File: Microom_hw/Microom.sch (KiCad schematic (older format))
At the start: 56 parts

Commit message: Sch 50% complete
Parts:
- removed R? (x8): 200, symbol R
- added C? (x3): 0.1u, CAP_0603, symbol C
- added C? (x2): 1u, CAP_0603, symbol C
- added C? (x2): 10u, CAP_0603, symbol C
- added DA?: PCM1865, TSSOP30, symbol PCM1865
- added F?: Fuse0R, symbol Fuse0R
- added R? (x8): 510, symbol R
- added TP? (x9): TESTPOINT, symbol TESTPOINT
- R?: value 200 -> 510
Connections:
- net labels added: +3.3V_A, 1V8, AGND, BitClk, CS, DataOut, LRClk, MCO, MISO, MOSI, SCK, SCKI
- net labels removed: VAA
- wire segments 141 -> 187
- no-connect marks 31 -> 30
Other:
- note added: "I2S2 WS (NSS)"
- note added: "I2S_MCK"
- note added: "No Crystal"
- note added: "SPI"
- moved on the sheet: R?

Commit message: Sch 100% completed
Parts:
- removed HOLE?: HOLE_METALLED, symbol HOLE_METALLED
- added C21, C28, C31: 2.2u, CAP_0603, symbol C
- added C22, C23, C29, C32, C33: 0.1u, CAP_0603, symbol C
- added C26: 1u, CAP_0603, symbol C
- added C27, C35: 10u, CAP_0603, symbol C
- added C36, C37, C38, C39, C40, C41, C42, C43: 10n, CAP_0603, symbol C
- added C44, C45, C46, C47, C48, C49, C50, C51: 10u, CAP_0805, symbol C
- added DA4: PCM1865, TSSOP30, symbol PCM1865
- added MIC1, MIC2, MIC3, MIC4, MIC5, MIC6, MIC7, MIC8: Microphone, symbol Microphone
- added R14, R15, R16, R17, R18, R19, R20, R21: 100R, RES_0603, symbol R
- added R22, R23, R24, R25, R26, R27, R28, R29: 2.2k, RES_0603, symbol R
- added R30, R31, R32, R33, R34, R35, R36, R37: 100k, RES_0603, symbol R
- added TP1, TP11, TP12, TP13, TP14, TP15, TP16, TP17, TP18, TP19, TP20: TESTPOINT, symbol TESTPOINT
- C18: renamed from C?; value 1u -> 2.2u
- gave numbers to parts that had none: 72
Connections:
- net +3.3V_A: now also C23.1, C27.1, C33.1, C35.1, DA4.13 (DVDD), DA4.14 (IOVDD), DA4.26 (MD0), DA4.8 (AVDD)
- net 1V8: now also C22.1, C26.1, DA4.11 (LDO)
- net AGND: now also C21.2, C22.2, C23.2, C26.2, C27.2, C28.2, C29.2, C31.2, C32.2, C33.2, C35.2, C36.2, C37.2, C38.2, C39.2, C40.2, C41.2, C42.2, C43.2, DA4.10 (XI), DA4.12 (DGND), DA4.7 (AGND), MIC1.2, MIC2.2, MIC3.2, MIC4.2, MIC5.2, MIC6.2, MIC7.2, MIC8.2, R30.2, R31.2, R32.2, R33.2, R34.2, R35.2, R36.2, R37.2
- net GND: no longer HOLE1.H, HOLE2.H, HOLE3.H
- net LED1: now also DD1.9 ((ADC123-11)/PC1)
- net LED2: now also DD1.10 ((ADC123-12)/MISO2/PC2)
- net LED3: now also DD1.11 ((ADC123-13)/MOSI2/PC3)
- net LED4: now also DD1.24 ((ADC12-14)/PC4)
- net LED5: now also DD1.25 ((ADC12-15)/PC5)
- net LED6: now also DD1.38 (T8C2/RX6/T3C2/SDIO_D7/PC7)
- net LED7: now also DD1.39 (T8C3/T3C3/CK6/SDIO_D0/PC8)
- net LED8: now also DD1.2 (PC13)
- net LED_AUX: now also DD1.8 ((ADC123-10)/PC0)
- net MISO: now also DA4.22 (MISO/GPIO0/DMIN2)
- net MOSI: now also DA4.23 (MOSI/SDA)
- net SCK: now also DA4.24 (MC/SCL)
- net SCKI: now also DA4.15 (SCKI)
- net GPIO22: now reaches DD1.14 ((ADC123-0)/TX4/T5C1/WKUP/PA0)
- net GPIO22: now also DA4.20 (GPIO2/IntB/DMCLK), TP19.1
- net GPIO32: now reaches DD1.15 ((ADC123-1)/RX4/T5C2/T2C2/PA1)
- net GPIO32: now also DA4.19 (GPIO3/IntC), TP20.1
- net CS2: now reaches DD1.17 ((ADC123-3)/T5C4/T9C2/T2C4/RX2/PA3)
- net CS2: now also DA4.25 (MS/AD), TP17.1
- net GPIO21: now reaches DD1.26 (PB0/T3C3/(ADC12-8))
- net GPIO21: now also DA3.20 (GPIO2/IntB/DMCLK), TP12.1
- net GPIO31: now reaches DD1.27 (PB1/T3C4/(ADC12-9))
- net GPIO31: now also DA3.19 (GPIO3/IntC), TP13.1
- net GPIO11: now reaches DD1.35 (PB14/MISO2/T12C1)
- net GPIO11: now also DA3.21 (GPIO1/IntA/DMIN), TP11.1
- net MCO2: now reaches DD1.40 (MCO2/T8C4/SDA3/T3C4/SDIO_D1/PC9)
- net MCO2: now also TP1.1
- net LRClk2: now reaches DD1.50 (PA15)
- net LRClk2: now also DA4.16 (LRCK), TP14.1
- net BitClk2: now reaches DD1.51 (SCK3/TX4/TX3/SDIO_D2/PC10)
- net BitClk2: now also DA4.17 (BCK), TP15.1
- net GPIO12: now reaches DD1.52 (MISO3/RX4/RX3/SDIO_D3/PC11)
- net GPIO12: now also DA4.21 (GPIO1/IntA/DMIN), TP18.1
- net DataOut2: now reaches DD1.53 (MOSI3/TX5/CK3/SDIO_CK/PC12)
- net DataOut2: now also DA4.18 (DOUT), TP16.1
- net VinL2: now reaches DA3.1 (VinL2)
- net VinL2: now also C38.1, R16.2
- net VinR2: now reaches DA3.2 (VinR2)
- net VinR2: now also C39.1, R17.2
- net VinL4: now reaches DA3.27 (VinL4)
- net VinL4: now also C42.1, DA4.27 (VinL4), R20.2
- net VinR4: now reaches DA3.28 (VinR4)
- net VinR4: now also C43.1, DA4.28 (VinR4), R21.2
- net VinL3: now reaches DA3.29 (VinL3)
- net VinL3: now also C40.1, DA4.29 (VinL3), R18.2
- net VinL1: now reaches DA3.3 (VinL1)
- net VinL1: now also C36.1, R14.2
- net VinR3: now reaches DA3.30 (VinR3)
- net VinR3: now also C41.1, DA4.30 (VinR3), R19.2
- net VinR1: now reaches DA3.4 (VinR1)
- net VinR1: now also C37.1, R15.2
- net MicBias: now reaches DA3.5 (MicBias)
- net MicBias: now also C28.1, C29.1, R22.2, R23.2, R24.2, R25.2, R26.2, R27.2, R28.2, R29.2
- net BitClk renamed BitClk1
- net CS renamed CS1
- net DataOut renamed DataOut1
- net LRClk renamed LRClk1
- net MCO renamed MCO1
- new net: C44.2, MIC1.1, R22.1, R30.1
- new net: C44.1, R14.1
- new net: C45.2, MIC2.1, R23.1, R31.1
- new net: C45.1, R15.1
- new net: C46.2, MIC3.1, R24.1, R32.1
- new net: C46.1, R16.1
- new net: C47.2, MIC4.1, R25.1, R33.1
- new net: C47.1, R17.1
- new net: C48.2, MIC5.1, R26.1, R34.1
- new net: C48.1, R18.1
- new net: C49.2, MIC6.1, R27.1, R35.1
- new net: C49.1, R19.1
- new net: C50.2, MIC7.1, R28.1, R36.1
- new net: C50.1, R20.1
- new net: C51.2, MIC8.1, R29.1, R37.1
- new net: C51.1, R21.1
- new net: C21.1, DA4.6 (Vref)
- new net MicBias2: C31.1, C32.1, DA4.5 (MicBias)
- no-connect marks 30 -> 23
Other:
- note added: "Audio converters"
- note added: "I2S3 WS (NSS)"
- note added: "Indication and mounting"
- note added: "MCU"
- note added: "Microphones"
- moved on the sheet: C1, C10, C11, C18, C19, C2, C20, C24, C25, C3, C30, C34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

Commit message: PCB routing started, components put on board
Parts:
- removed VCap1, VCap2: 2.2u, symbol C
- added C52, C53: 2.2u, Capacitors:CAP_0603, symbol C
- C1: footprint (none) -> Capacitors:CAP_0805
- C10, C11, C14, C15, C16, C17, C2, C3, C4, C6, C8, C9: footprint (none) -> Capacitors:CAP_0603
- C13, C5, C7: footprint Capacitors:CAP_0402 -> Capacitors:CAP_0603
- C18, C19, C20, C21, C22, C23, C24, C26, C28, C29, C30, C31, C32, C33, C36, C37, C38, C39, C40, C41, C42, C43: footprint CAP_0603 -> Capacitors:CAP_0603
- C25, C27, C34, C35: footprint CAP_0603 -> Capacitors:CAP_0805
- C44, C45, C46, C47, C48, C49, C50, C51: footprint CAP_0805 -> Capacitors:CAP_0805
- D1, D2, D3, D4, D5, D6, D7, D8, D9: footprint (none) -> LEDs:LED_0603
- DA1, DA2: footprint (none) -> SOT:SOT23-5
- DA3, DA4: footprint TSSOP30 -> SO_DIL_TSSOP:TSSOP30
- DD1: footprint (none) -> LQFP_TQFP:LQFP64
- F1: footprint (none) -> Resistors:RES_0603_SOLDERFUSE
- HOLE1, HOLE2, HOLE3: footprint (none) -> PCB:Hole3_5_out6mm
- MIC1, MIC2, MIC3, MIC4, MIC5, MIC6, MIC7, MIC8: footprint (none) -> Connectors:PLS-2
- R1: footprint Resistors:RES_0402 -> Resistors:RES_0603
- R10, R11, R12, R13, R2, R3, R5, R6, R7, R8, R9: footprint (none) -> Resistors:RES_0603
- R14, R15, R16, R17, R18, R19, R20, R21, R22, R23, R24, R25, R26, R27, R28, R29, R30, R31, R32, R33, R34, R35, R36, R37, R4: footprint RES_0603 -> Resistors:RES_0603
- SW1: footprint (none) -> BtnsSwitches:BTN_6x6
- TP1, TP10, TP11, TP12, TP13, TP14, TP15, TP16, TP17, TP18, TP19, TP2, TP20, TP3, TP4, TP5, TP6, TP7, TP8, TP9: footprint (none) -> PCB:TESTPOINT_1MM
- XL1: footprint ~ -> Connectors:PLS-3
- XL3: footprint ~ -> Connectors:PLS-4
- XTAL1: footprint CRYSTAL -> Quartz:0503x4-4
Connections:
- net GND: now also C52.1, C53.1
- net at DD1.31 (VCap1): now also C52.2
- net at DD1.47 (VCap2): now also C53.2

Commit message: * Components spread over the board
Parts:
- removed C29, C32: 0.1u, Capacitors:CAP_0603, symbol C
- removed R3, R4: 1k, Resistors:RES_0603, symbol R
- removed SW1: BUTTON, BtnsSwitches:BTN_6x6, symbol BUTTON
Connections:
- net +3.3V: now also DD1.42 ((OTGFS_VBUS)/T1C2/TX1/PA9)
- net GND: now also DD1.60 (BOOT0)
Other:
- moved on the sheet: C28, C31

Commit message: * PCB routing 30% completed
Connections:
- net 1V8: no longer C22.1, C26.1, DA4.11 (LDO)
- net AGND: now also D2.C, D3.C, D4.C, D5.C, D6.C, D7.C, D8.C, D9.C
- net GND: no longer D2.C, D3.C, D4.C, D5.C, D6.C, D7.C, D8.C, D9.C
- new net 1V8_2: C22.1, C26.1, DA4.11 (LDO)

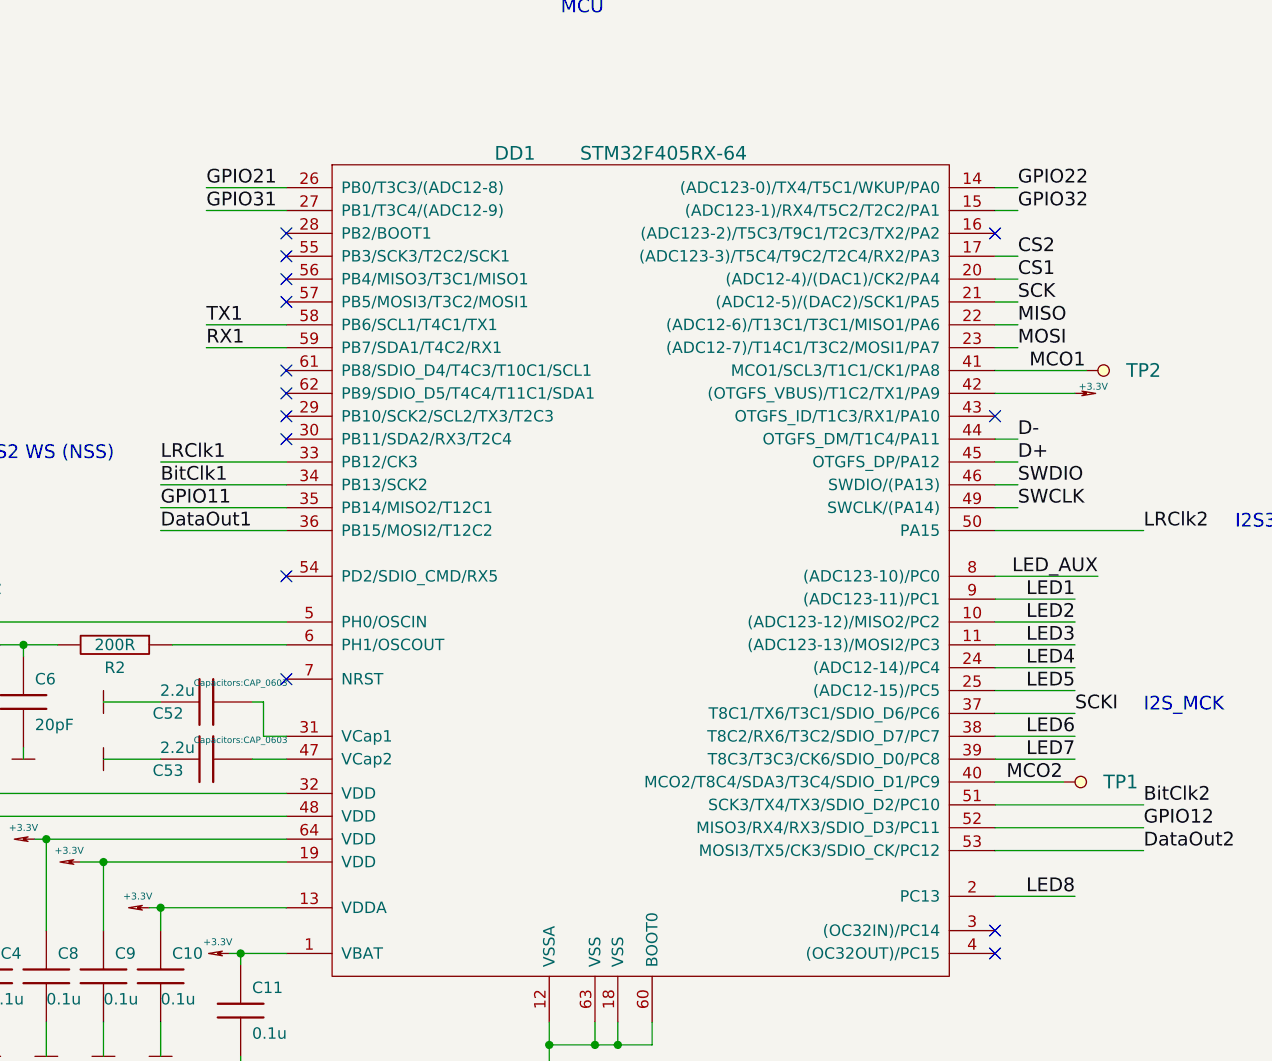
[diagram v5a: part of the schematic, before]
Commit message: Routing done, GND planes not placed yet.
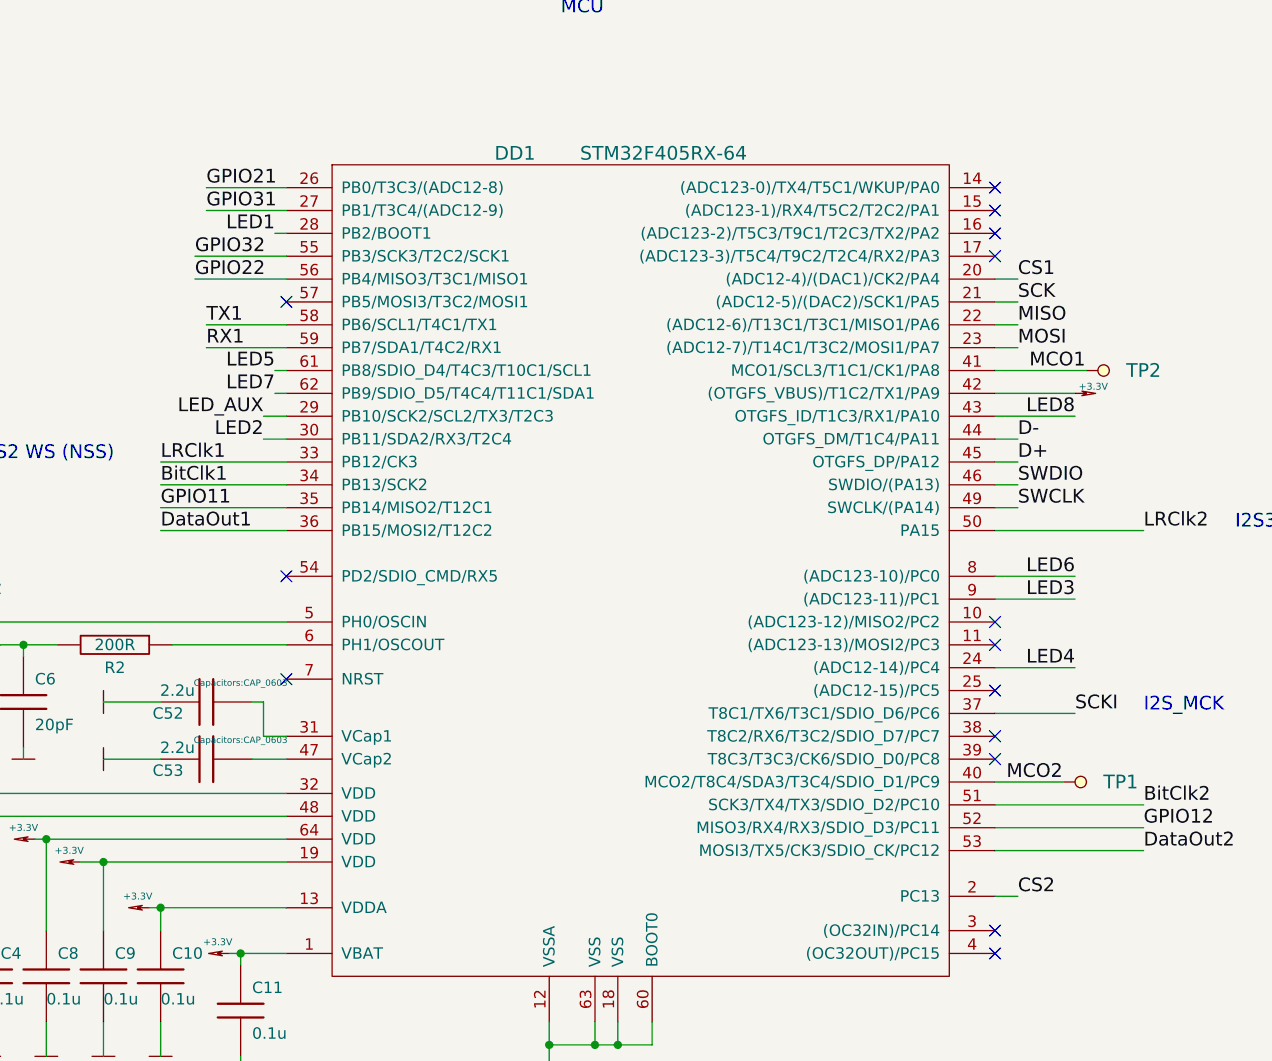
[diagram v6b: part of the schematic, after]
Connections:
- net CS2: now also DD1.2 (PC13); no longer DD1.17 ((ADC123-3)/T5C4/T9C2/T2C4/RX2/PA3)
- net GPIO22: now also DD1.56 (PB4/MISO3/T3C1/MISO1); no longer DD1.14 ((ADC123-0)/TX4/T5C1/WKUP/PA0)
- net GPIO32: now also DD1.55 (PB3/SCK3/T2C2/SCK1); no longer DD1.15 ((ADC123-1)/RX4/T5C2/T2C2/PA1)
- net LED1: now also DD1.28 (PB2/BOOT1); no longer DD1.9 ((ADC123-11)/PC1)
- net LED2: now also DD1.30 (PB11/SDA2/RX3/T2C4); no longer DD1.10 ((ADC123-12)/MISO2/PC2)
- net LED3: now also DD1.9 ((ADC123-11)/PC1); no longer DD1.11 ((ADC123-13)/MOSI2/PC3)
- net LED5: now also DD1.61 (PB8/SDIO_D4/T4C3/T10C1/SCL1); no longer DD1.25 ((ADC12-15)/PC5)
- net LED6: now also DD1.8 ((ADC123-10)/PC0); no longer DD1.38 (T8C2/RX6/T3C2/SDIO_D7/PC7)
- net LED7: now also DD1.62 (PB9/SDIO_D5/T4C4/T11C1/SDA1); no longer DD1.39 (T8C3/T3C3/CK6/SDIO_D0/PC8)
- net LED8: now also DD1.43 (OTGFS_ID/T1C3/RX1/PA10); no longer DD1.2 (PC13)
- net LED_AUX: now also DD1.29 (PB10/SCK2/SCL2/TX3/T2C3); no longer DD1.8 ((ADC123-10)/PC0)
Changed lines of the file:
@@
 $EndComp
 NoConn ~ 2800 3650
-NoConn ~ 2800 1700
-NoConn ~ 2800 2300
-NoConn ~ 2800 2400
-NoConn ~ 2800 2500
-NoConn ~ 2800 2600
 NoConn ~ 2800 3200
 NoConn ~ 5900 4850
@@
 Wire Wire Line
 	11050 1950 10900 1950
-Text Label 6250 3300 2    60   ~ 0
+Text Label 2750 1700 2    60   ~ 0
 LED1
-Text Label 6250 3400 2    60   ~ 0
+Text Label 2700 2600 2    60   ~ 0
 LED2
-Text Label 6250 3500 2    60   ~ 0
+Text Label 6250 3300 2    60   ~ 0
 LED3
 Text Label 6250 3600 2    60   ~ 0
 LED4
-Text Label 6250 3700 2    60   ~ 0
+Text Label 2750 2300 2    60   ~ 0
 LED5
-Text Label 6250 3900 2    60   ~ 0
+Text Label 6250 3200 2    60   ~ 0
 LED6
-Text Label 6250 4000 2    60   ~ 0
+Text Label 2750 2400 2    60   ~ 0
 LED7
-Text Label 6250 4600 2    60   ~ 0
+Text Label 6250 2500 2    60   ~ 0
 LED8
 Wire Wire Line
 	6250 3300 5900 3300
 Wire Wire Line
-	5900 3400 6250 3400
-Wire Wire Line
-	6250 3500 5900 3500
-Wire Wire Line
 	6250 3600 5900 3600
 Wire Wire Line
-	5900 3700 6250 3700
-Wire Wire Line
-	6250 3900 5900 3900
+	6250 3200 5900 3200
 Wire Wire Line
-	5900 4000 6250 4000
-Wire Wire Line
-	6250 4600 5900 4600
-Text Label 6350 3200 2    60   ~ 0
+	6250 2500 5900 2500
+Text Label 2700 2500 2    60   ~ 0
 LED_AUX
 Wire Wire Line
-	6350 3200 5900 3200
-Wire Wire Line
 	11400 1900 11750 1900
 Wire Wire Line
@@
 Text Label 5950 4100 0    60   ~ 0
 MCO2
-NoConn ~ 5900 2500
 Wire Notes Line
 	8700 7300 8700 11200
@@
 	10900 5400 11550 5400
 Connection ~ 11400 5400
-Text Label 6000 1800 0    60   ~ 0
+Text Label 6000 4600 0    60   ~ 0
 CS2
 Wire Wire Line
-	6000 1800 5900 1800
+	6000 4600 5900 4600
 NoConn ~ 10900 4550
 NoConn ~ 10900 4650
 NoConn ~ 10900 4750
 NoConn ~ 10900 4850
-Text Label 6000 1600 0    60   ~ 0
+Text Label 2400 1800 0    60   ~ 0
 GPIO32
-Text Label 6000 1500 0    60   ~ 0
+Text Label 2400 1900 0    60   ~ 0
 GPIO22
 Wire Wire Line
-	5900 1500 6000 1500
-Wire Wire Line
-	6000 1600 5900 1600
-NoConn ~ 2800 1800
-NoConn ~ 2800 1900
-NoConn ~ 2800 2000
-Wire Wire Line
 	9000 4550 9300 4550
 Wire Wire Line
@@
 Wire Wire Line
 	6850 8150 6850 9700
+Wire Wire Line
+	2700 2600 2800 2600
+Wire Wire Line
+	2700 2500 2800 2500
+Wire Wire Line
+	2750 1700 2800 1700
+Wire Wire Line
+	2400 1800 2800 1800
+Wire Wire Line
+	2800 1900 2400 1900
+Wire Wire Line
+	2750 2400 2800 2400
+Wire Wire Line
+	2750 2300 2800 2300
+NoConn ~ 5900 1800
+NoConn ~ 5900 1500
+NoConn ~ 5900 1600
+NoConn ~ 2800 2000
+NoConn ~ 5900 3400
+NoConn ~ 5900 3500
+NoConn ~ 5900 3700
+NoConn ~ 5900 3900
+NoConn ~ 5900 4000
 $EndSCHEMATC

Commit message: Minor changes
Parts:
- XL2: symbol USB_MINI_B -> USB_MINI_B-RESCUE-Microom
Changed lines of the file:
@@
 EESchema Schematic File Version 2
+LIBS:Microom-rescue
 LIBS:pcb_details
 LIBS:power
@@
 $EndComp
 $Comp
-L USB_MINI_B XL2
+L USB_MINI_B-RESCUE-Microom XL2
 U 1 1 55D3B305
 P 1400 8500
